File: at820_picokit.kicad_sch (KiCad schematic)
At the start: 26 parts, among them J1 SWD, J2 download, J3 I2C, J4 uart0, J5 SPI0, J6 power, SW3 SW_Push, SW5 SW_Push_DPDT, U2 CH343P, Y2 Crystal_GND24

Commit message: update file format to kicad 10.0
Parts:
- U4: value ~ -> (none)

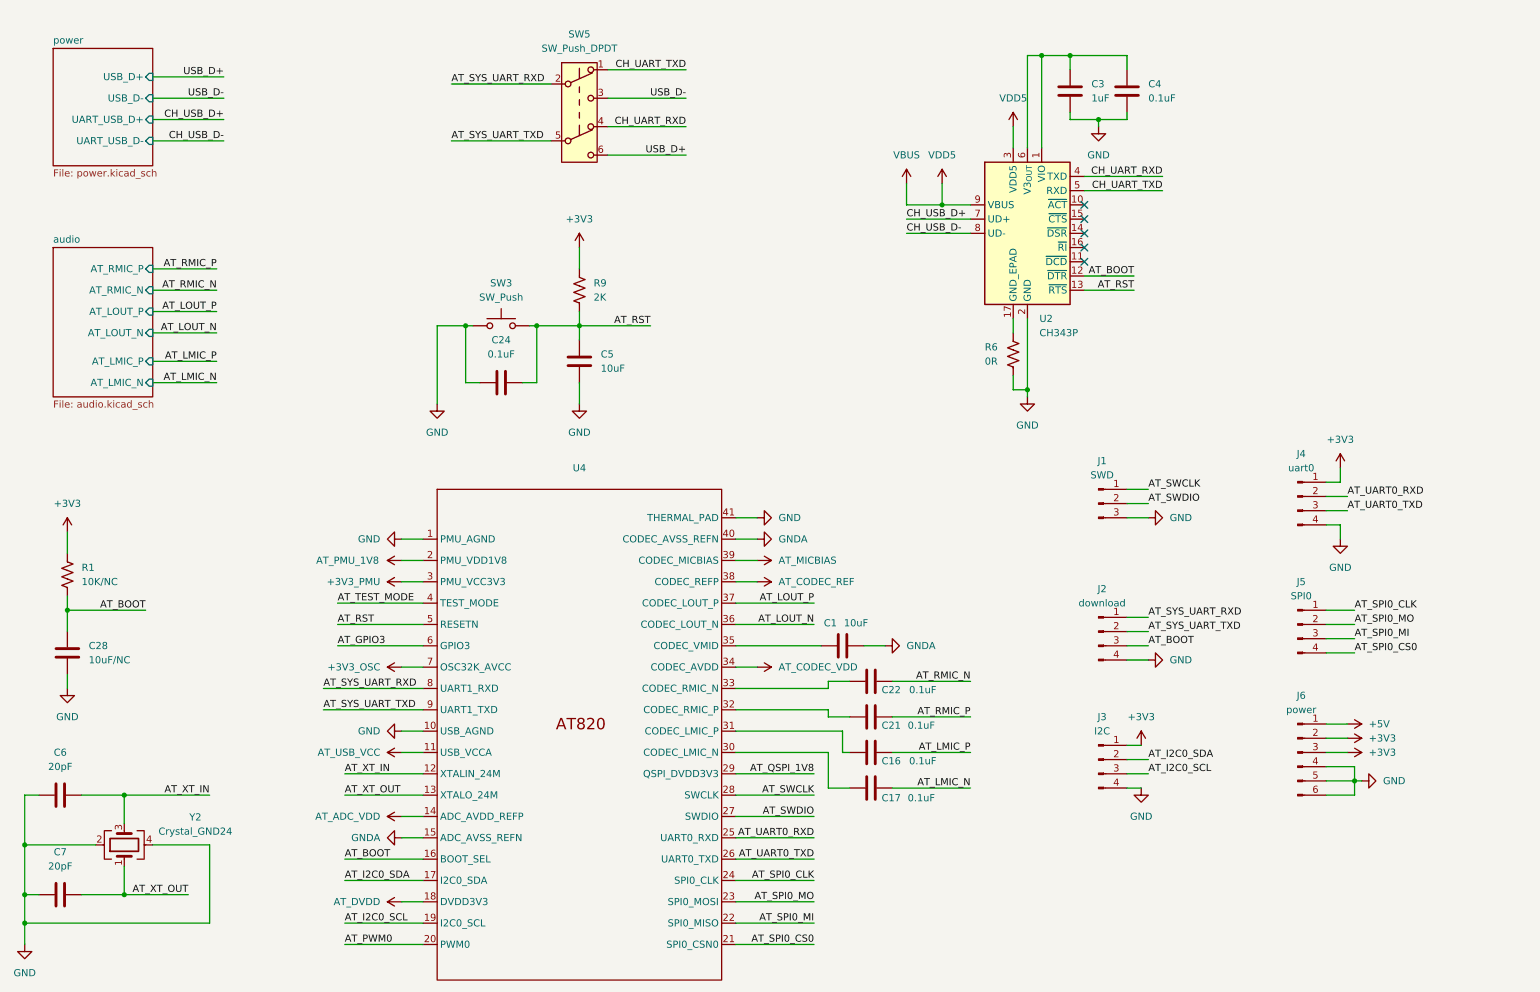
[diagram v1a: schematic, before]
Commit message: fix at820 sym, impl audio pa
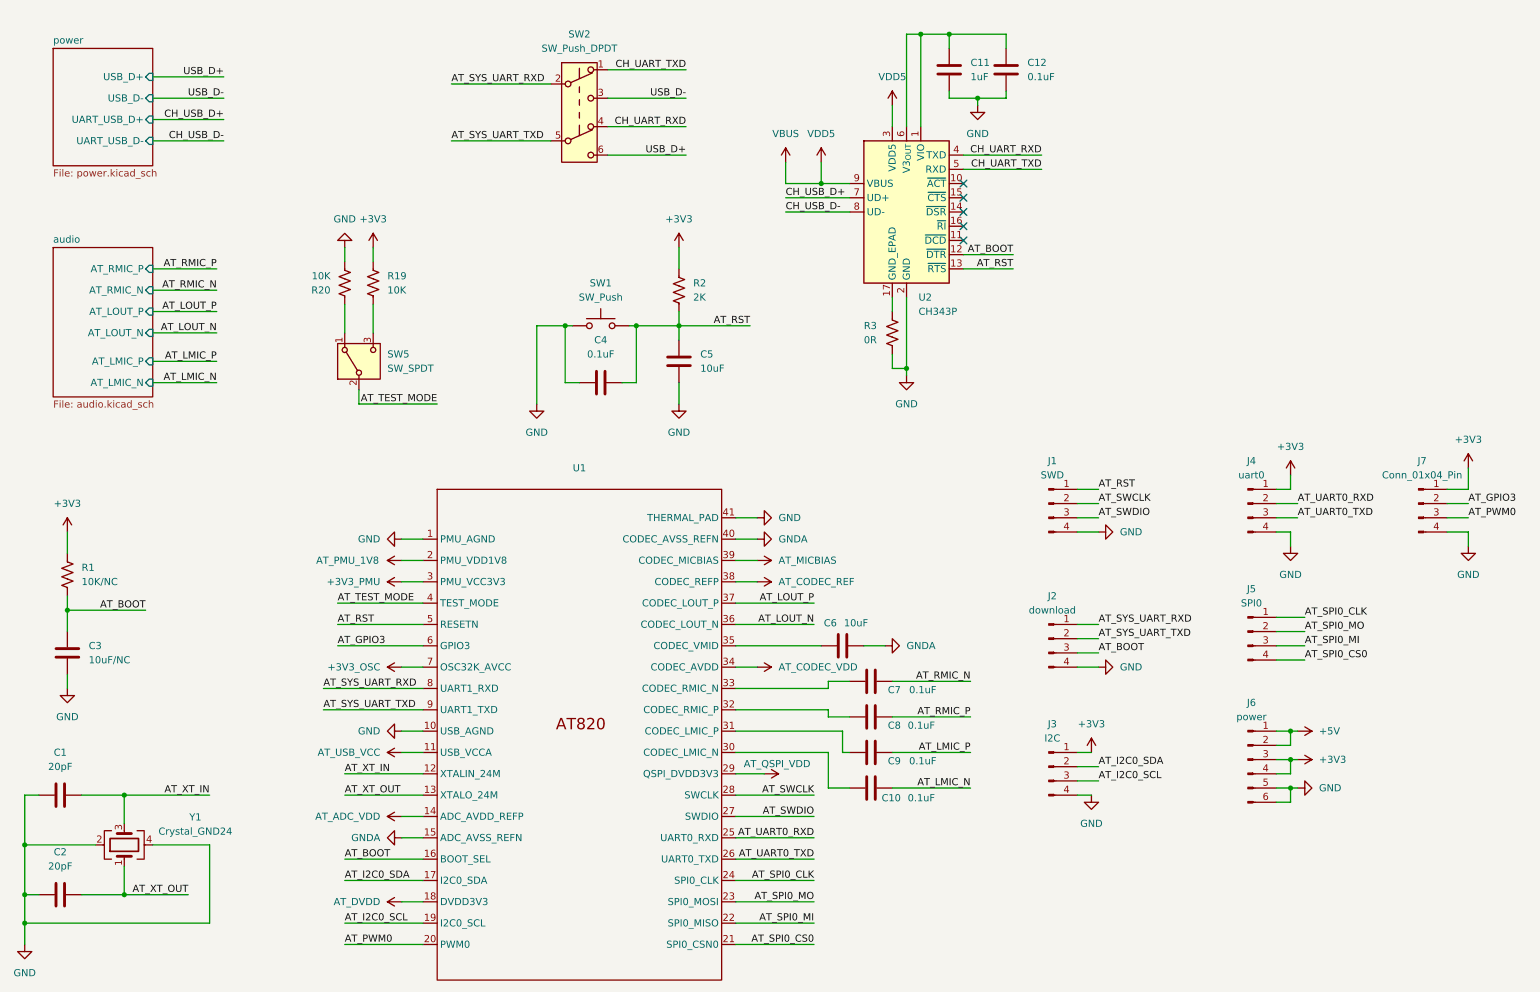
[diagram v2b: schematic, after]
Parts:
- removed J1: SWD, symbol Connector:Conn_01x03_Pin
- added J1: SWD, symbol Connector:Conn_01x04_Pin
- added J7: Conn_01x04_Pin, symbol Connector:Conn_01x04_Pin
- added R19, R20: 10K, symbol Device:R_US
- added SW5: SW_SPDT, Button_Switch_SMD:Nidec_Copal_CAS-120A, symbol Switch:SW_SPDT
- renumbered C6 to C1, C17 to C10, C3 to C11, C4 to C12, C7 to C2, C28 to C3, C24 to C4, C1 to C6, C22 to C7, C21 to C8, C16 to C9, R9 to R2, R6 to R3, SW3 to SW1, SW5 to SW2, U4 to U1, Y2 to Y1
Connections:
- net +3V3: now also J6.4 (Pin_4), J7.1 (Pin_1), R19.1; no longer J6.2 (Pin_2)
- net +5V: now also J6.2 (Pin_2)
- net AT_GPIO3: now also J7.2 (Pin_2)
- net AT_PWM0: now also J7.3 (Pin_3)
- net AT_RST: now also J1.1 (Pin_1)
- net AT_SWCLK: now also J1.2 (Pin_2)
- net AT_SWDIO: now also J1.3 (Pin_3)
- net AT_TEST_MODE: now also SW5.2 (B)
- net GND: now also J1.4 (Pin_4), J7.4 (Pin_4), R20.2; no longer J6.4 (Pin_4)
- net AT_QSPI_1V8 renamed AT_QSPI_VDD
- new net: R20.1, SW5.1 (A)
- new net: R19.2, SW5.3 (C)
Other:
- moved on the sheet: C11, C12, C4, C5, J2, J3, J4, J5, J6, R2, R3, SW1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

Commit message: sch features done, all drc passed
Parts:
- added C4, C7: 0.1uF, symbol Device:C
- added SW2: Wakeup Button, symbol Switch:SW_Push
- SW3: renamed from SW1; value SW_Push -> Reset Button
- renumbered C3 to C1, C7 to C10, C8 to C11, C9 to C12, C10 to C13, C12 to C14, C1 to C2, C2 to C3, C4 to C5, C5 to C6, C6 to C8, C11 to C9, R20 to R2, R19 to R3, R2 to R4, R3 to R5, SW5 to SW1, SW2 to SW4
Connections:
- net AT_GPIO3: now also C4.2, SW2.2
- net AT_XT_IN: now also Y1.1; no longer Y1.3
- net AT_XT_OUT: now also Y1.3; no longer Y1.1
- net GND: now also C4.1, C7.2, SW2.1
- net VBUS: now also C7.1
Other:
- sheet audio ports: added PA_EN; removed none
- moved on the sheet: C1, C14, C2, C3, C5, C6, C9, J1, J2, J3, J4, J5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

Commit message: asigning footprint
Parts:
- C1, C10, C11, C12, C13, C14, C2, C3, C4, C5, C6, C7, C8, C9: footprint (none) -> Capacitor_SMD:C_0603_1608Metric_Pad1.08x0.95mm_HandSolder
- R1, R2, R3, R4, R5: footprint (none) -> Resistor_SMD:R_0603_1608Metric_Pad0.98x0.95mm_HandSolder
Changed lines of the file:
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@@
 			)
 		)
-		(property "Footprint" ""
+		(property "Footprint" "Capacitor_SMD:C_0603_1608Metric_Pad1.08x0.95mm_HandSolder"
 			(at 165.1 150.8252 0)
 			(hide yes)
@@
 			)
 		)
-		(property "Footprint" ""
+		(property "Footprint" "Resistor_SMD:R_0603_1608Metric_Pad0.98x0.95mm_HandSolder"
 			(at 45.974 119.126 90)
 			(hide yes)
@@
 			)
 		)
-		(property "Footprint" ""
+		(property "Footprint" "Capacitor_SMD:C_0603_1608Metric_Pad1.08x0.95mm_HandSolder"
 			(at 29.21 164.7952 0)
 			(hide yes)
@@
 			)
 		)
-		(property "Footprint" ""
+		(property "Footprint" "Capacitor_SMD:C_0603_1608Metric_Pad1.08x0.95mm_HandSolder"
 			(at 176.2252 30.48 0)
 			(hide yes)
@@
 			)
 		)
-		(property "Footprint" ""
+		(property "Footprint" "Capacitor_SMD:C_0603_1608Metric_Pad1.08x0.95mm_HandSolder"
 			(at 22.5552 135.89 0)
 			(hide yes)
@@
 			)
 		)
-		(property "Footprint" ""
+		(property "Footprint" "Capacitor_SMD:C_0603_1608Metric_Pad1.08x0.95mm_HandSolder"
 			(at 91.44 34.5948 0)
 			(hide yes)
@@
 			)
 		)
-		(property "Footprint" ""
+		(property "Footprint" "Capacitor_SMD:C_0603_1608Metric_Pad1.08x0.95mm_HandSolder"
 			(at 160.02 131.7752 0)
 			(hide yes)
@@
 			)
 		)
-		(property "Footprint" ""
+		(property "Footprint" "Resistor_SMD:R_0603_1608Metric_Pad0.98x0.95mm_HandSolder"
 			(at 153.924 73.406 90)
 			(hide yes)
@@
 			)
 		)
-		(property "Footprint" ""
+		(property "Footprint" "Resistor_SMD:R_0603_1608Metric_Pad0.98x0.95mm_HandSolder"
 			(at 102.616 62.484 90)
 			(hide yes)
@@
 			)
 		)
-		(property "Footprint" ""
+		(property "Footprint" "Resistor_SMD:R_0603_1608Metric_Pad0.98x0.95mm_HandSolder"
 			(at 53.086 119.634 90)
 			(hide yes)
@@
 			)
 		)
-		(property "Footprint" ""
+		(property "Footprint" "Capacitor_SMD:C_0603_1608Metric_Pad1.08x0.95mm_HandSolder"
 			(at 91.44 77.7748 0)
 			(hide yes)
@@
 			)
 		)
-		(property "Footprint" ""
+		(property "Footprint" "Resistor_SMD:R_0603_1608Metric_Pad0.98x0.95mm_HandSolder"
 			(at 22.606 118.364 90)
 			(hide yes)
@@
 			)
 		)
-		(property "Footprint" ""
+		(property "Footprint" "Capacitor_SMD:C_0603_1608Metric_Pad1.08x0.95mm_HandSolder"
 			(at 166.0652 30.48 0)
 			(hide yes)
@@
 			)
 		)
-		(property "Footprint" ""
+		(property "Footprint" "Capacitor_SMD:C_0603_1608Metric_Pad1.08x0.95mm_HandSolder"
 			(at 165.1 157.1752 0)
 			(hide yes)
@@
 			)
 		)
-		(property "Footprint" ""
+		(property "Footprint" "Capacitor_SMD:C_0603_1608Metric_Pad1.08x0.95mm_HandSolder"
 			(at 143.2052 39.37 0)
 			(hide yes)
@@
 			)
 		)
-		(property "Footprint" ""
+		(property "Footprint" "Capacitor_SMD:C_0603_1608Metric_Pad1.08x0.95mm_HandSolder"
 			(at 165.1 138.1252 0)
 			(hide yes)
@@
 			)
 		)
-		(property "Footprint" ""
+		(property "Footprint" "Capacitor_SMD:C_0603_1608Metric_Pad1.08x0.95mm_HandSolder"
 			(at 29.21 182.5752 0)
 			(hide yes)
@@
 			)
 		)
-		(property "Footprint" ""
+		(property "Footprint" "Capacitor_SMD:C_0603_1608Metric_Pad1.08x0.95mm_HandSolder"
 			(at 165.1 144.4752 0)
 			(hide yes)
@@
 			)
 		)
-		(property "Footprint" ""
+		(property "Footprint" "Capacitor_SMD:C_0603_1608Metric_Pad1.08x0.95mm_HandSolder"
 			(at 102.5652 78.74 0)
 			(hide yes)

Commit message: refactor some switch circuit
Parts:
- J1, J2, J3, J4, J5, J6, J7: footprint (none) -> Connector_PinHeader_2.54mm:PinHeader_1x04_P2.54mm_Vertical
- SW2, SW3: footprint (none) -> Button_Switch_SMD:SW_SPST_PTS810
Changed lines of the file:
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@@
 			)
 		)
-		(property "Footprint" ""
+		(property "Footprint" "Connector_PinHeader_2.54mm:PinHeader_1x04_P2.54mm_Vertical"
 			(at 224.79 93.98 0)
 			(hide yes)
@@
 			)
 		)
-		(property "Footprint" ""
+		(property "Footprint" "Connector_PinHeader_2.54mm:PinHeader_1x04_P2.54mm_Vertical"
 			(at 224.79 71.12 0)
 			(hide yes)
@@
 			)
 		)
-		(property "Footprint" ""
+		(property "Footprint" "Connector_PinHeader_2.54mm:PinHeader_1x04_P2.54mm_Vertical"
 			(at 189.23 118.11 0)
 			(hide yes)
@@
 			)
 		)
-		(property "Footprint" ""
+		(property "Footprint" "Connector_PinHeader_2.54mm:PinHeader_1x04_P2.54mm_Vertical"
 			(at 224.79 116.84 0)
 			(hide yes)
@@
 			)
 		)
-		(property "Footprint" ""
+		(property "Footprint" "Button_Switch_SMD:SW_SPST_PTS810"
 			(at 87.63 63.5 0)
 			(hide yes)
@@
 			)
 		)
-		(property "Footprint" ""
+		(property "Footprint" "Connector_PinHeader_2.54mm:PinHeader_1x04_P2.54mm_Vertical"
 			(at 189.23 95.25 0)
 			(hide yes)
@@
 			)
 		)
-		(property "Footprint" ""
+		(property "Footprint" "Connector_PinHeader_2.54mm:PinHeader_1x04_P2.54mm_Vertical"
 			(at 260.35 72.39 0)
 			(hide yes)
@@
 			)
 		)
-		(property "Footprint" ""
+		(property "Footprint" "Button_Switch_SMD:SW_SPST_PTS810"
 			(at 87.63 24.13 0)
 			(hide yes)
@@
 			)
 		)
-		(property "Footprint" ""
+		(property "Footprint" "Connector_PinHeader_2.54mm:PinHeader_1x04_P2.54mm_Vertical"
 			(at 189.23 71.12 0)
 			(hide yes)

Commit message: sch all done, footprint done
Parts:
- removed SW4: SW_Push_DPDT, symbol Switch:SW_Push_DPDT
- added R6: 10K, Resistor_SMD:R_0603_1608Metric_Pad0.98x0.95mm_HandSolder, symbol Device:R_US
- added SW4: SW_SPST, Connector_PinHeader_2.54mm:PinHeader_1x02_P2.54mm_Vertical, symbol Switch:SW_SPST
- added U3: TS5A23157DGS, Package_SO:TSSOP-10_3x3mm_P0.5mm, symbol Analog_Switch:TS5A23157DGS
- renumbered C11 to C10, C12 to C11, C13 to C12, C14 to C13, C9 to C14, C10 to C9
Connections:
- net +3V3: now also SW4.2 (B), U3.8 (VCC)
- net AT_SYS_UART_RXD: now also U3.10
- net AT_SYS_UART_TXD: now also U3.6
- net CH_UART_RXD: now also U3.7
- net CH_UART_TXD: now also U3.9
- net GND: now also R6.1, U3.3 (GND)
- net USB_D+: now also U3.4
- net USB_D-: now also U3.2
- new net: R6.2, SW4.1 (A), U3.1, U3.5
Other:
- moved on the sheet: C13, C14, C2, C3, C4, C5, C6, C7, J1, J2, J3, J4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

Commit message: components loc done, pcb ing
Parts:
- removed R6: 10K, Resistor_SMD:R_0603_1608Metric_Pad0.98x0.95mm_HandSolder, symbol Device:R_US
- removed SW4: SW_SPST, Connector_PinHeader_2.54mm:PinHeader_1x02_P2.54mm_Vertical, symbol Switch:SW_SPST
- added C36: 0.1uF, Capacitor_SMD:C_0603_1608Metric_Pad1.08x0.95mm_HandSolder, symbol Device:C
- added J13: TEST_MODE, Connector_PinHeader_2.54mm:PinHeader_1x02_P2.54mm_Vertical, symbol Connector:Conn_01x02_Pin
- added SW6: Boot Button, Button_Switch_SMD:SW_SPST_PTS810, symbol Switch:SW_Push
- J6: footprint Connector_PinHeader_2.54mm:PinHeader_1x04_P2.54mm_Vertical -> Connector_PinHeader_2.54mm:PinHeader_1x06_P2.54mm_Vertical
- SW1: value SW_SPDT -> OS102011MS2QN1; footprint Button_Switch_SMD:Nidec_Copal_CAS-120A -> Button_Switch_THT:SW_Slide_SPDT_Straight_CK_OS102011MS2Q
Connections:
- net +3V3: now also J3.4 (Pin_4), J4.4 (Pin_4), J7.4 (Pin_4), SW1.3 (C); no longer J3.1 (Pin_1), J4.1 (Pin_1), J7.1 (Pin_1)
- net +5V: now also J6.5 (Pin_5), J6.6 (Pin_6); no longer J6.1 (Pin_1), J6.2 (Pin_2)
- net AT_BOOT: now also J2.4 (Pin_4), C36.2, SW6.2; no longer J2.3 (Pin_3)
- net AT_RST: now also J1.2 (Pin_2); no longer J1.1 (Pin_1)
- net AT_SWCLK: now also J1.3 (Pin_3); no longer J1.2 (Pin_2)
- net AT_SWDIO: now also J1.4 (Pin_4); no longer J1.3 (Pin_3)
- net AT_SYS_UART_RXD: now also J2.2 (Pin_2); no longer J2.1 (Pin_1)
- net AT_SYS_UART_TXD: now also J2.3 (Pin_3); no longer J2.2 (Pin_2)
- net AT_TEST_MODE: now also R2.1, J13.1 (Pin_1); no longer SW1.2 (B)
- net GND: now also J1.1 (Pin_1), J2.1 (Pin_1), J3.1 (Pin_1), J4.1 (Pin_1), J6.1 (Pin_1), J6.2 (Pin_2), J7.1 (Pin_1), SW1.1 (A), C36.1, SW6.1; no longer J1.4 (Pin_4), J2.4 (Pin_4), J3.4 (Pin_4), J4.4 (Pin_4), J6.5 (Pin_5), J6.6 (Pin_6), J7.4 (Pin_4)
- net at U3.1, U3.5: now also SW1.2 (B)
- net at R3.2: now also J13.2 (Pin_2); no longer SW1.3 (C)
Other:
- moved on the sheet: C4, SW2, U3C
